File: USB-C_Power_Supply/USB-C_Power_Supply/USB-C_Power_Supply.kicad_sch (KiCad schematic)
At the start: 60 parts, among them J1 USB_C_Receptacle_USB2.0_16P, J2 Screw_Terminal_01x02, J3 Conn_01x03_Pin, Q1 2N7002, Q2 PMOS, SW1 SW_DIP_x03, U2 USBLC6-2P6, U3 CH224A, U4 MC14051BDR2G, U5 MCP16331x-xCH

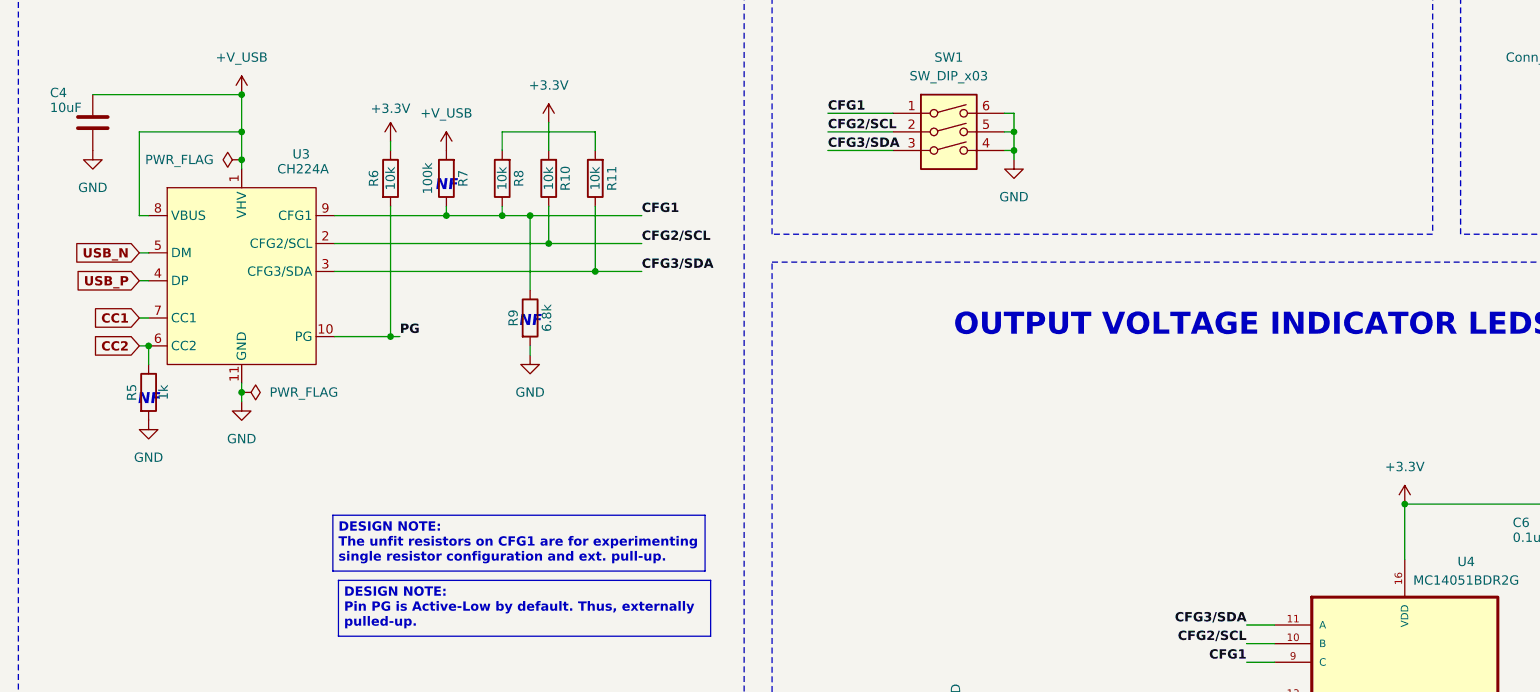
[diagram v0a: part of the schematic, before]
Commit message: Footprint assigned
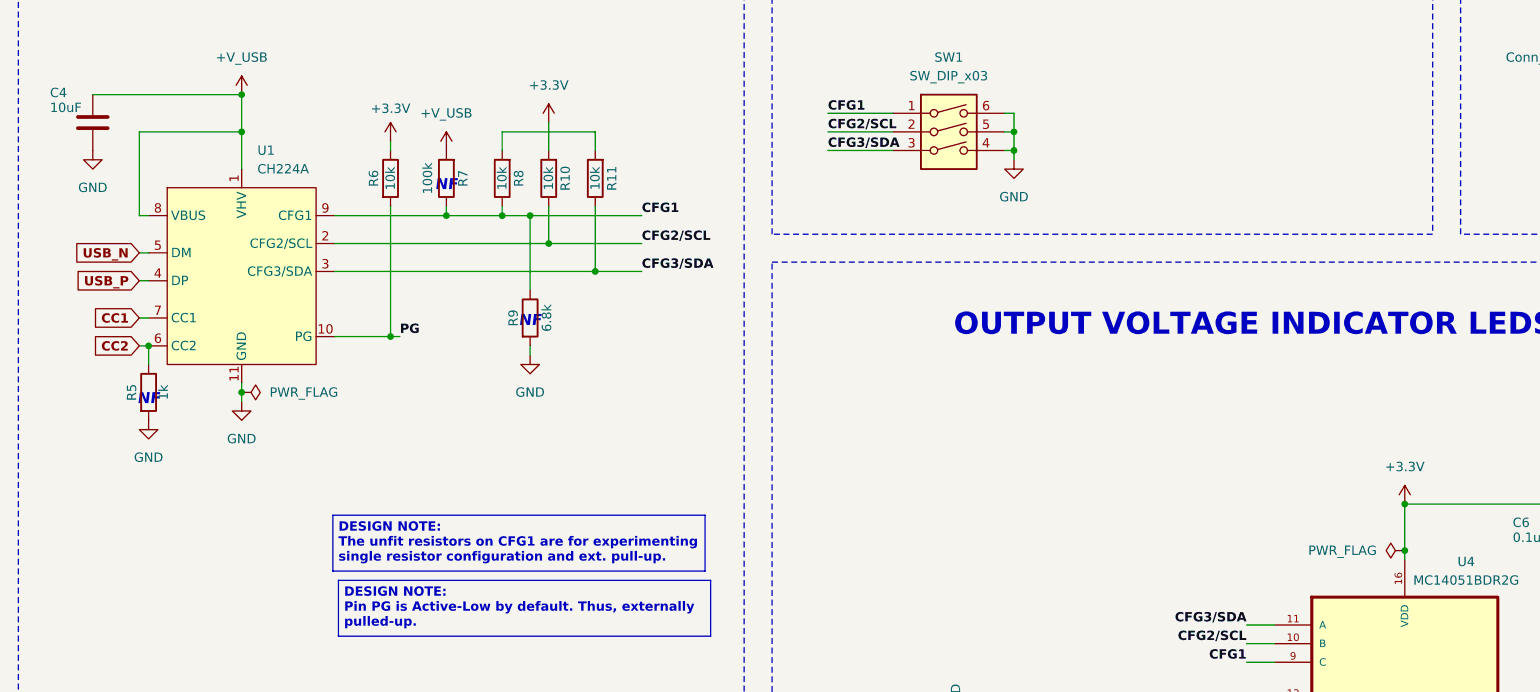
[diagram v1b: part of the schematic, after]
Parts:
- removed U3: CH224A, CH224A:CH224A USB PD Multi Fast Charging Protocol Power Receiving Chip, symbol CH224A:CH224A_USB_PD_Multi_Fast_Charging_Protocol_Power_Receiving_Chip
- added U1: CH224A, CH224A:CH224A USB PD Multi Fast Charging Protocol Power Receiving Chip, symbol CH224A:CH224A_USB_PD_Multi_Fast_Charging_Protocol_Power_Receiving_Chip
- C10: footprint (none) -> Capacitor_SMD:C_0805_2012Metric
- C11, C12, C13, C16, C5, C6, C9: footprint (none) -> Capacitor_SMD:C_0603_1608Metric
- C14, C15, C2, C4, C7: footprint (none) -> Capacitor_SMD:C_1206_3216Metric
- C8: footprint (none) -> Capacitor_SMD:C_1210_3225Metric
- D1, D2, D3, D4, D5, D6: footprint (none) -> LED_SMD:LED_0603_1608Metric
- D7: footprint (none) -> Diode_SMD:D_SOD-123
- D8: footprint (none) -> Diode_SMD:D_SMB
- H1, H2, H3, H4: footprint (none) -> MountingHole:MountingHole_2.5mm_Pad
- J2: footprint (none) -> Screw Terminal:CUI_TB007-508-02BE
- J3: footprint (none) -> Connector_PinHeader_2.54mm:PinHeader_1x03_P2.54mm_Vertical
- L1: footprint (none) -> Inductor_SMD:L_6.3x6.3_H3
- Q2: footprint (none) -> Package_TO_SOT_SMD:SOT-23
- SW1: footprint (none) -> Button_Switch_SMD:SW_DIP_SPSTx03_Slide_6.7x9.18mm_W8.61mm_P2.54mm_LowProfile
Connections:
- net +V_USB: now also U1.1 (VHV), U1.11 (GND), U1.8 (VBUS)
- net CC1: now also U1.7 (CC1)
- net CC2: now also U1.6 (CC2)
- net CFG1: now also U1.9 (CFG1)
- net CFG2/SCL: now also U1.2 (CFG2/SCL)
- net CFG3/SDA: now also U1.3 (CFG3/SDA)
- net PG: now also U1.10 (PG)
- net USB_N: now also U1.5 (DM)
- net USB_P: now also U1.4 (DP)

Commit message: Footprints assigned
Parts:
- J1: footprint (none) -> Connector_USB:USB_C_Receptacle_GCT_USB4105-xx-A_16P_TopMnt_Horizontal
- U1: footprint CH224A:CH224A USB PD Multi Fast Charging Protocol Power Receiving Chip -> CH224A:CH224A
- U4: footprint MC14051BDR2G:SOIC127P600X175-16N -> MC14051BDR2G:MC14051BDR2G
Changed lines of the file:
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@@
 			)
 		)
-		(property "Footprint" "CH224A:CH224A USB PD Multi Fast Charging Protocol Power Receiving Chip"
+		(property "Footprint" "CH224A:CH224A"
 			(at 171.958 61.976 0)
 			(hide yes)
@@
 			)
 		)
-		(property "Footprint" ""
+		(property "Footprint" "Connector_USB:USB_C_Receptacle_GCT_USB4105-xx-A_16P_TopMnt_Horizontal"
 			(at 50.8 72.39 0)
 			(hide yes)
@@
 			)
 		)
-		(property "Footprint" "MC14051BDR2G:SOIC127P600X175-16N"
+		(property "Footprint" "MC14051BDR2G:MC14051BDR2G"
 			(at 342.138 119.634 0)
 			(hide yes)

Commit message: PCB Layout started
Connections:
- net +V_USB: no longer C10.2, C11.2, C14.2, C15.2, C16.2, C2.2, C4.2, C5.2, C6.2, C7.2, C8.2, C9.2, D2.1 (K), D3.1 (K), D4.1 (K), D5.1 (K), D6.1 (K), D8.1 (A1), D9.2 (A), H1.1, H2.1, H3.1, H4.1, J1.A1 (GND), J1.A12 (GND), J1.B1 (GND), J1.B12 (GND), J2.2 (Pin_2), J3.2 (Pin_2), Q1.2 (S), R17.1, R18.1, R22.1, R5.2, R9.2, SW1.4, SW1.5, SW1.6, U1.11 (GND), U2.2 (GND), U4.7 (VEE), U4.8 (VSS), U5.2 (GND)
- net VBUS: now reaches D8.2 (A2), J1.A4 (VBUS), J1.A9 (VBUS), J1.B4 (VBUS), J1.B9 (VBUS), Q2.1 (D)
- new net GND: C10.2, C11.2, C14.2, C15.2, C16.2, C2.2, C4.2, C5.2, C6.2, C7.2, C8.2, C9.2, D2.1 (K), D3.1 (K), D4.1 (K), D5.1 (K), D6.1 (K), D8.1 (A1), D9.2 (A), H1.1, H2.1, H3.1, H4.1, J1.A1 (GND), J1.A12 (GND), J1.B1 (GND), J1.B12 (GND), J2.2 (Pin_2), J3.2 (Pin_2), Q1.2 (S), R17.1, R18.1, R22.1, R5.2, R9.2, SW1.4, SW1.5, SW1.6, U1.11 (GND), U2.2 (GND), U4.7 (VEE), U4.8 (VSS), U5.2 (GND)
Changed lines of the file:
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@@
 	)
 	(junction
-		(at 46.99 177.8)
-		(diameter 0)
-		(color 0 0 0 0)
-	)
-	(junction
 		(at 340.36 172.72)
 		(diameter 0)
@@
 	(wire
 		(pts
-			(xy 181.61 57.15) (xy 181.61 62.23)
-		)
-		(stroke
-			(width 0)
-			(type default)
-		)
-	)
-	(wire
-		(pts
 			(xy 274.32 165.1) (xy 279.4 165.1)
 		)
@@
 	(wire
 		(pts
+			(xy 181.61 57.15) (xy 181.61 62.23)
+		)
+		(stroke
+			(width 0)
+			(type default)
+		)
+	)
+	(wire
+		(pts
 			(xy 62.23 71.12) (xy 62.23 72.39)
 		)
@@
 	(wire
 		(pts
-			(xy 46.99 170.18) (xy 46.99 177.8)
-		)
-		(stroke
-			(width 0)
-			(type default)
-		)
-	)
-	(wire
-		(pts
 			(xy 342.9 172.72) (xy 342.9 171.45)
 		)
@@
 		)
 	)
+	(label "VBUS"
+		(at 63.5 57.15 0)
+		(effects
+			(font
+				(size 1.27 1.27)
+			)
+			(justify left bottom)
+		)
+	)
 	(label "CFG3{slash}SDA"
 		(at 236.22 81.28 0)
@@
 					(unit 1)
 				)
+			)
+		)
+	)
+	(symbol
+		(lib_id "power:PWR_FLAG")
+		(at 181.61 62.23 270)
+		(unit 1)
+		(body_style 1)
+		(exclude_from_sim no)
+		(in_bom yes)
+		(on_board yes)
+		(in_pos_files yes)
+		(dnp no)
+		(fields_autoplaced yes)
+		(property "Reference" "#FLG05"
+			(at 183.515 62.23 0)
+			(hide yes)
+			(show_name no)
+			(do_not_autoplace no)
+			(effects
+				(font
+					(size 1.27 1.27)
+				)
+			)
+		)
+		(property "Value" "PWR_FLAG"
+			(at 185.42 62.2299 90)
+			(show_name no)
+			(do_not_autoplace no)
+			(effects
+				(font
+					(size 1.27 1.27)
+				)
+				(justify left)
+			)
+		)
+		(property "Footprint" ""
+			(at 181.61 62.23 0)
+			(hide yes)
+			(show_name no)
+			(do_not_autoplace no)
+			(effects
+				(font
+					(size 1.27 1.27)
+				)
+			)
+		)
+		(property "Datasheet" ""
+			(at 181.61 62.23 0)
+			(hide yes)
+			(show_name no)
+			(do_not_autoplace no)
+			(effects
+				(font
+					(size 1.27 1.27)
+				)
+			)
+		)
+		(property "Description" "Special symbol for telling ERC where power comes from"
+			(at 181.61 62.23 0)
+			(hide yes)
+			(show_name no)
+			(do_not_autoplace no)
+			(effects
+				(font
+					(size 1.27 1.27)
+				)
+			)
+		)
+		(pin "1"
+		)
+		(instances
+			(project "USB-C_Power_Supply"
+				(path "/07987bcc-2856-4164-8b3e-c1534058717d"
+					(reference "#FLG05")
+					(unit 1)
+				)
